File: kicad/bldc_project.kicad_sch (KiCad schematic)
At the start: 0 parts

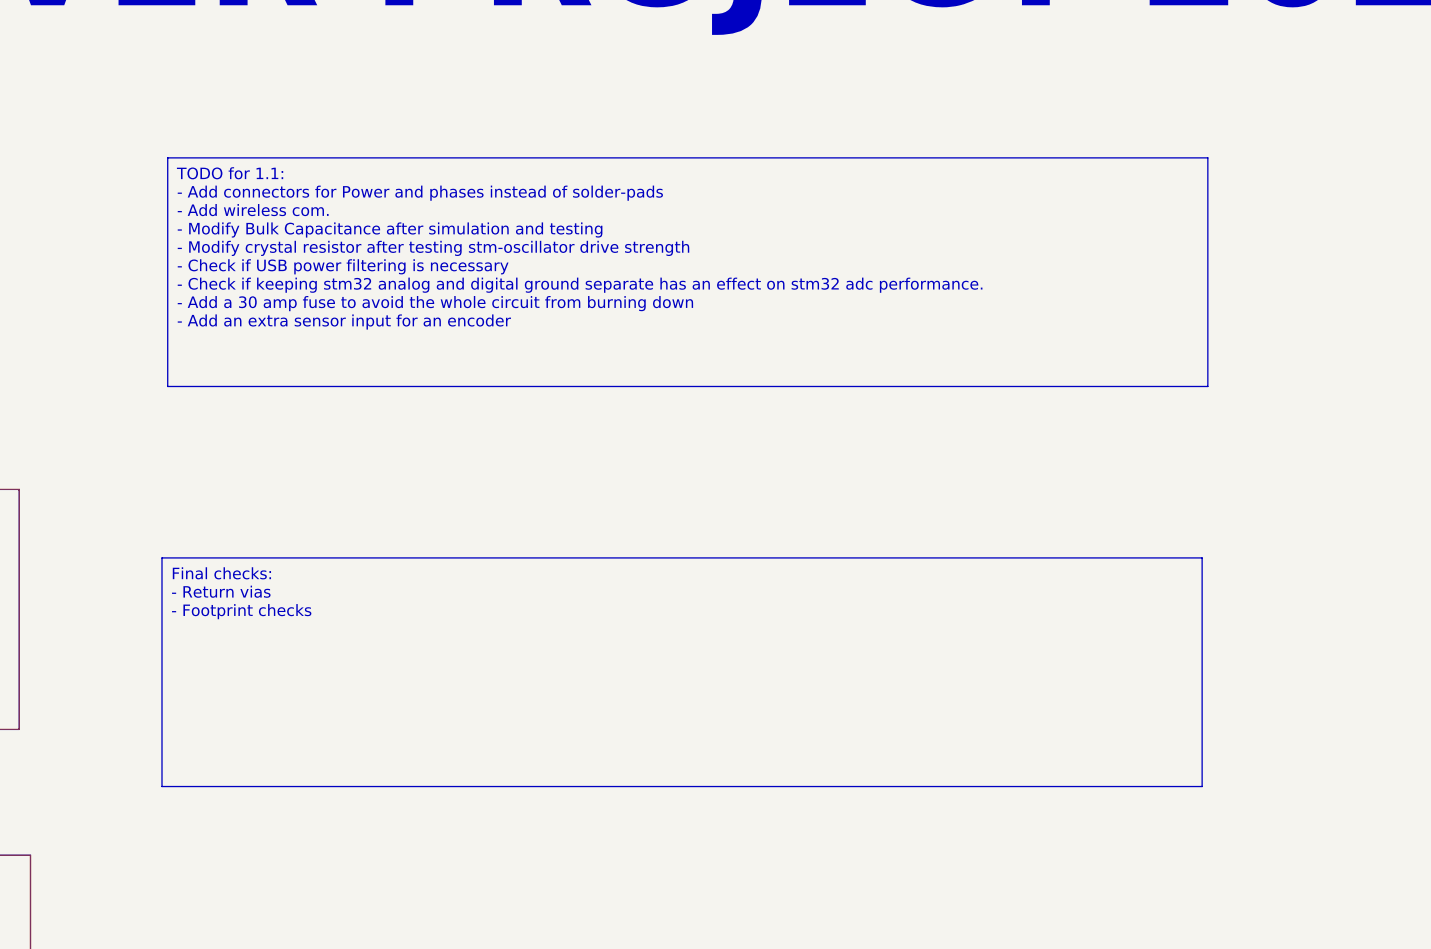
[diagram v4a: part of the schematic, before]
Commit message: [kicad] Added different ESD protection device, silkscreen indication on the back, [review] Added pdf file and images of the front and back as well as 3d images
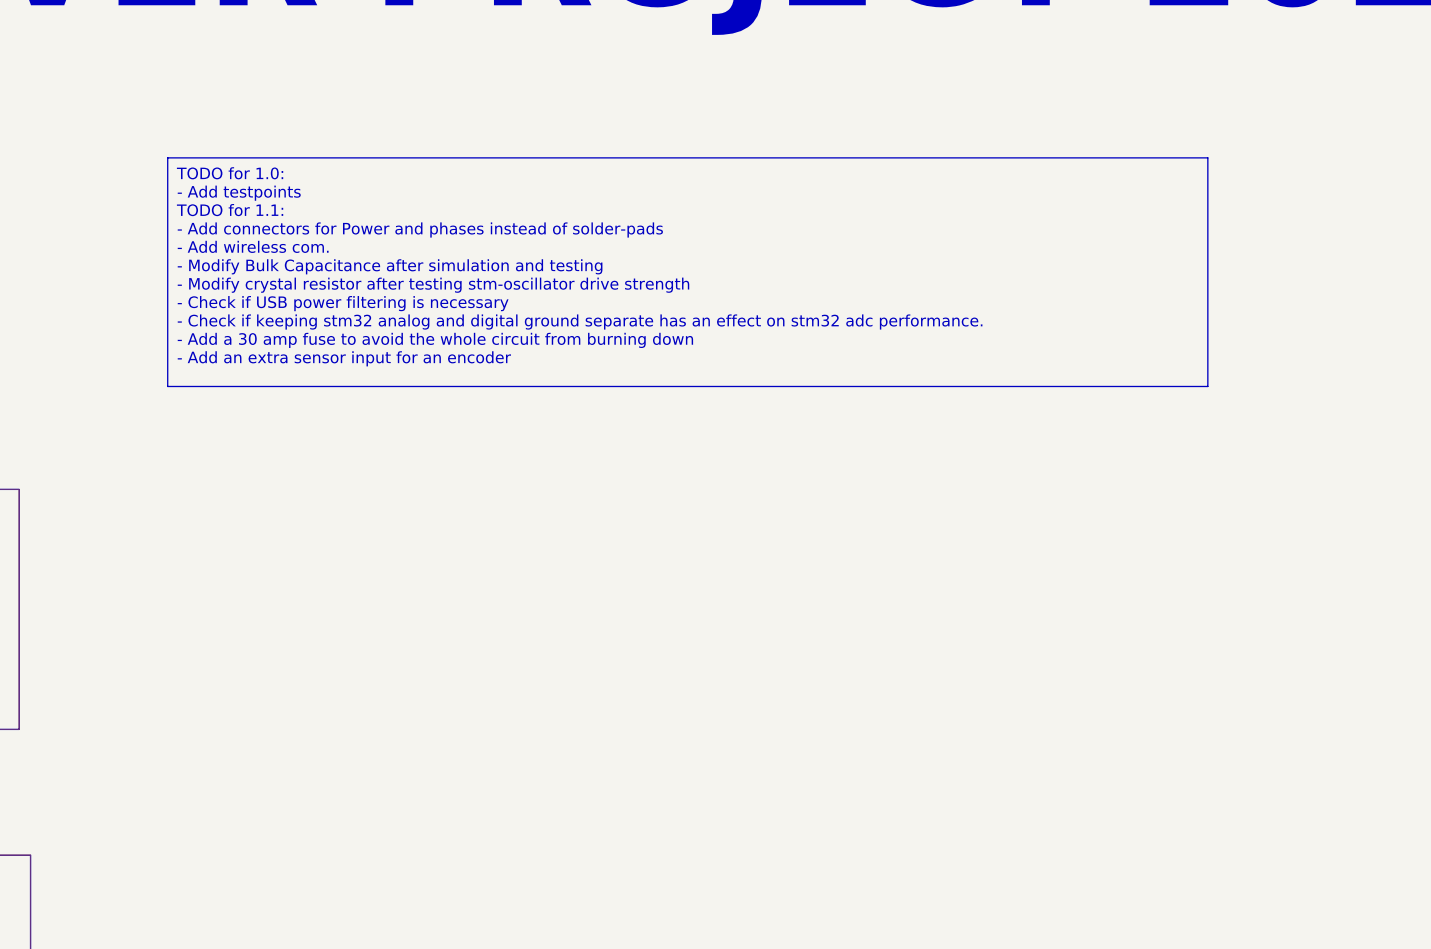
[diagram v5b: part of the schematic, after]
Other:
- company: Igor Wolfs -> IW
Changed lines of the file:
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@@
     (title "BLDC Driver Project")
     (rev "1.0")
-    (company "Igor Wolfs")
-    (comment 1 "fsad")
+    (company "IW")
   )
-  (text_box "Final checks:\n- Return vias\n- Footprint checks\n"
-    (at 123.825 93.98 0) (size 115.57 25.4)
-    (stroke (width 0) (type default))
-    (fill (type none))
-    (effects (font (size 1.27 1.27)) (justify left top))
-  )
-  (text_box "TODO for 1.1:\n- Add connectors for Power and phases instead of solder-pads\n- Add wireless com.\n- Modify Bulk Capacitance after simulation and testing\n- Modify crystal resistor after testing stm-oscillator drive strength\n- Check if USB power filtering is necessary\n- Check if keeping stm32 analog and digital ground separate has an effect on stm32 adc performance.\n- Add a 30 amp fuse to avoid the whole circuit from burning down\n- Add an extra sensor input for an encoder"
+  (text_box "TODO for 1.0:\n- Add testpoints\nTODO for 1.1:\n- Add connectors for Power and phases instead of solder-pads\n- Add wireless com.\n- Modify Bulk Capacitance after simulation and testing\n- Modify crystal resistor after testing stm-oscillator drive strength\n- Check if USB power filtering is necessary\n- Check if keeping stm32 analog and digital ground separate has an effect on stm32 adc performance.\n- Add a 30 amp fuse to avoid the whole circuit from burning down\n- Add an extra sensor input for an encoder"
     (at 124.46 49.53 0) (size 115.57 25.4)
     (stroke (width 0) (type default))
